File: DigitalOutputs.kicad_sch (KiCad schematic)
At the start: 2 parts, among them J12 DIGITAL_OUTPUTS

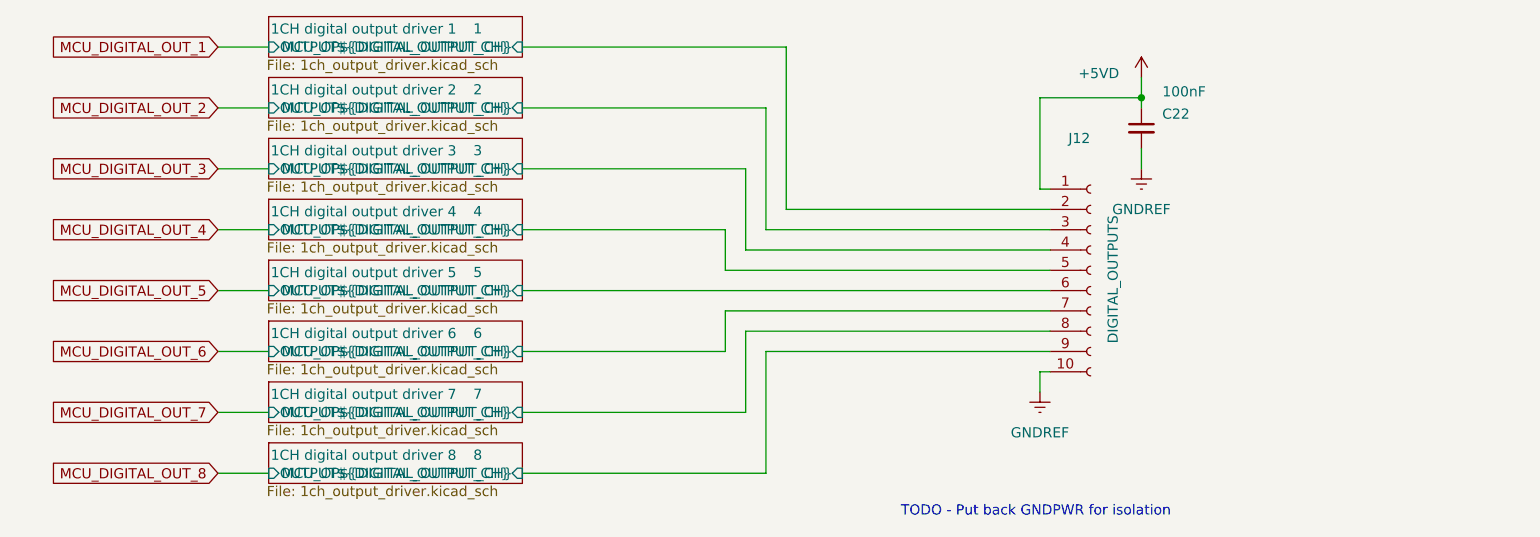
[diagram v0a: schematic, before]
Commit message: New optocoupler part choice, removed digikey BOM as have started inputting them into symbol fields. Re-enabled all disabled parts for now and will re-design power supplies soon.
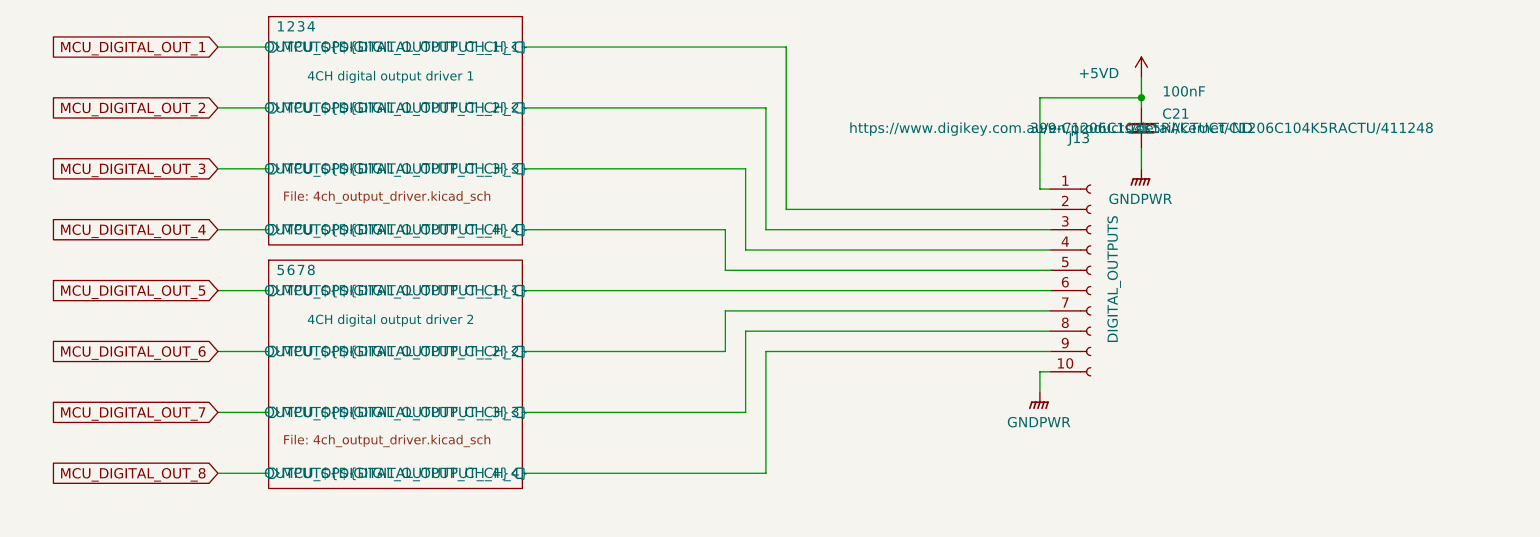
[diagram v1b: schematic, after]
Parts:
- C21: renamed from C22; Digikey Part Number (none) -> 399-C1206C104K5RACTUCT-ND; Digikey URL (none) -> https://www.digikey.com.au/en/products/detail/kemet/C1206C1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
- renumbered J12 to J13
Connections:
- net 4CH digital output driver 1/OUTPUT${DIGITAL_OUTPUT_CH} renamed 4CH digital output driver 1/OUTPUT${DIGITAL_OUTPUT_CH_1}
- net 1CH digital output driver 2/OUTPUT${DIGITAL_OUTPUT_CH} renamed 4CH digital output driver 1/OUTPUT${DIGITAL_OUTPUT_CH_2}
- net 1CH digital output driver 3/OUTPUT${DIGITAL_OUTPUT_CH} renamed 4CH digital output driver 1/OUTPUT${DIGITAL_OUTPUT_CH_3}
- net 1CH digital output driver 4/OUTPUT${DIGITAL_OUTPUT_CH} renamed 4CH digital output driver 1/OUTPUT${DIGITAL_OUTPUT_CH_4}
- net 1CH digital output driver 5/OUTPUT${DIGITAL_OUTPUT_CH} renamed 4CH digital output driver 2/OUTPUT${DIGITAL_OUTPUT_CH_1}
- net 1CH digital output driver 6/OUTPUT${DIGITAL_OUTPUT_CH} renamed 4CH digital output driver 2/OUTPUT${DIGITAL_OUTPUT_CH_2}
- net 1CH digital output driver 7/OUTPUT${DIGITAL_OUTPUT_CH} renamed 4CH digital output driver 2/OUTPUT${DIGITAL_OUTPUT_CH_3}
- net 1CH digital output driver 8/OUTPUT${DIGITAL_OUTPUT_CH} renamed 4CH digital output driver 2/OUTPUT${DIGITAL_OUTPUT_CH_4}
- net GNDREF renamed GNDPWR
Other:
- sheet 1CH digital output driver 1 renamed 4CH digital output driver 1
- removed sheet 1CH digital output driver 2
- removed sheet 1CH digital output driver 3
- removed sheet 1CH digital output driver 4
- removed sheet 1CH digital output driver 5
- removed sheet 1CH digital output driver 6
- removed sheet 1CH digital output driver 7
- removed sheet 1CH digital output driver 8
- added sheet 4CH digital output driver 2 (4ch_output_driver.kicad_sch)
- sheet 4CH digital output driver 1: file 1ch_output_driver.kicad_sch -> 4ch_output_driver.kicad_sch
- sheet 4CH digital output driver 1 ports: added MCU_OP${DIGITAL_OUTPUT_CH_1}, MCU_OP${DIGITAL_OUTPUT_CH_2}, MCU_OP${DIGITAL_OUTPUT_CH_3}, MCU_OP${DIGITAL_OUTPUT_CH_4}, OUTPUT${DIGITAL_OUTPUT_CH_1}, OUTPUT${DIGITAL_OUTPUT_CH_2}, OUTPUT${DIGITAL_OUTPUT_CH_3}, OUTPUT${DIGITAL_OUTPUT_CH_4}; removed MCU_OP${DIGITAL_OUTPUT_CH}, OUTPUT${DIGITAL_OUTPUT_CH}
- note removed: "TODO - Put back GNDPWR for isolation"

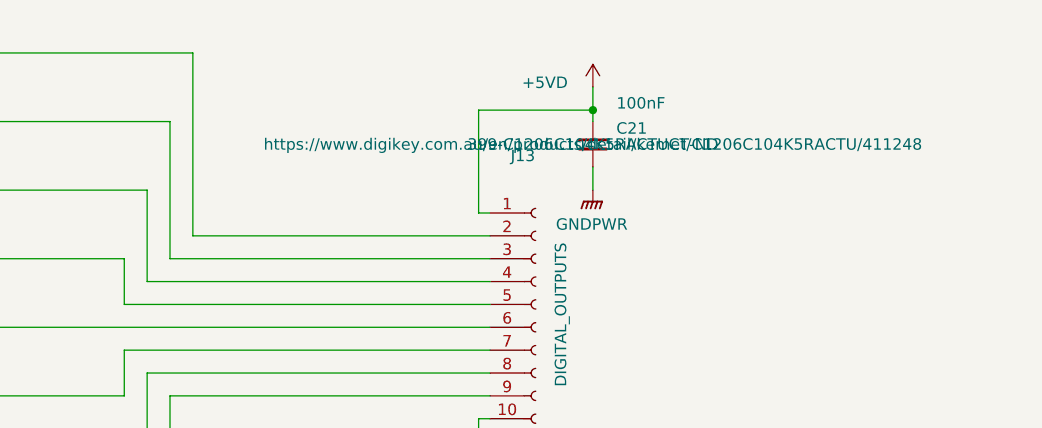
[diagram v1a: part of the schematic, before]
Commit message: fix to annoying additional symbol fields displaying when we didn't want them to.
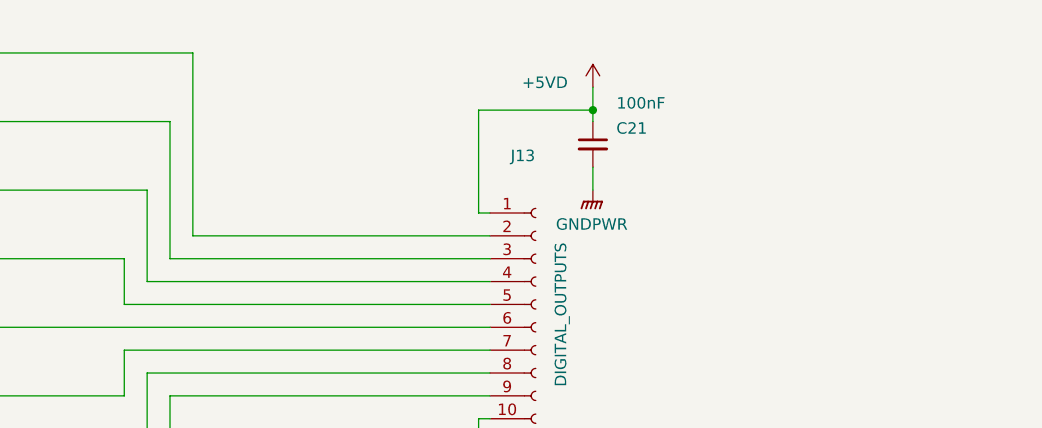
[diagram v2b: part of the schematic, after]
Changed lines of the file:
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@@
 					(size 1.27 1.27)
 				)
+				(hide yes)
 			)
 		)
@@
 					(size 1.27 1.27)
 				)
+				(hide yes)
 			)
 		)
@@
 					(size 1.27 1.27)
 				)
+				(hide yes)
 			)
 		)
@@
 					(size 1.27 1.27)
 				)
-			)
-		)
+				(hide yes)
+			)
+		)

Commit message: BOM consolidation for various resistors. Moved BOM into symbol libraries and updated supplimentary BOM. Switched IO optical isolation circuitry to a more cost effective part.
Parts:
- J13: Digikey Part Number (none) -> See Manual BOM; Digikey URL (none) -> See Manual BOM
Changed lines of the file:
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@@
 			)
 		)
-		(property "Digikey Part Number" ""
+		(property "Digikey Part Number" "See Manual BOM"
 			(at 205.74 93.98 0)
 			(effects
@@
 			)
 		)
-		(property "Digikey URL" ""
+		(property "Digikey URL" "See Manual BOM"
 			(at 205.74 93.98 0)
 			(effects

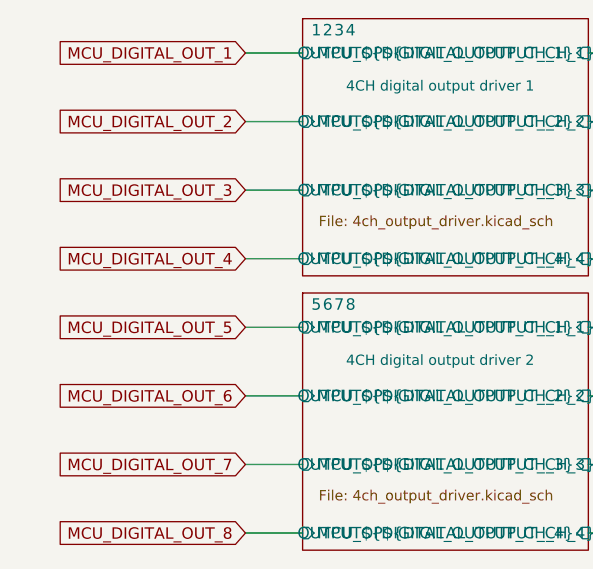
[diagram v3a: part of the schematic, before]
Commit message: Renumbered IO to start at 0 to match firmware
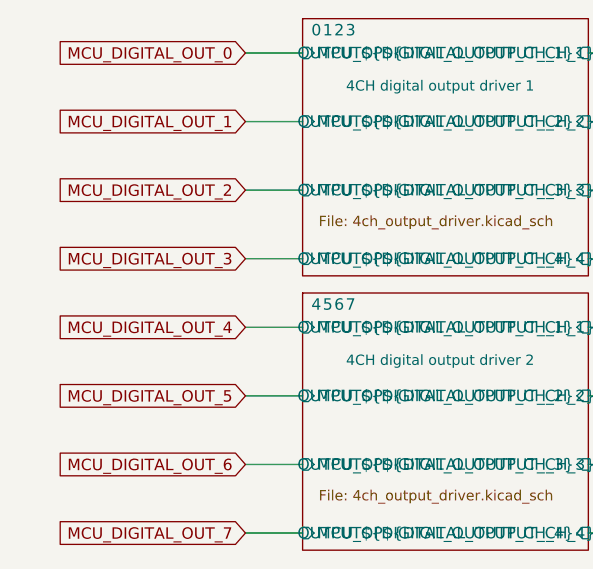
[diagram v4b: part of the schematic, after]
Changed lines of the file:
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@@
 	(global_label "MCU_DIGITAL_OUT_2"
 		(shape input)
-		(at 96.52 73.66 180)
+		(at 96.52 81.28 180)
 		(fields_autoplaced yes)
 		(effects
@@
 		)
 		(property "Intersheetrefs" "${INTERSHEET_REFS}"
-			(at 75.5623 73.66 0)
+			(at 75.5623 81.28 0)
 			(effects
 				(font
@@
 	(global_label "MCU_DIGITAL_OUT_3"
 		(shape input)
-		(at 96.52 81.28 180)
+		(at 96.52 88.9 180)
 		(fields_autoplaced yes)
 		(effects
@@
 		)
 		(property "Intersheetrefs" "${INTERSHEET_REFS}"
-			(at 75.5623 81.28 0)
+			(at 75.5623 88.9 0)
 			(effects
 				(font
@@
 	(global_label "MCU_DIGITAL_OUT_7"
 		(shape input)
-		(at 96.52 111.76 180)
+		(at 96.52 119.38 180)
 		(fields_autoplaced yes)
 		(effects
@@
 		)
 		(property "Intersheetrefs" "${INTERSHEET_REFS}"
-			(at 75.5623 111.76 0)
+			(at 75.5623 119.38 0)
 			(effects
 				(font
@@
 	(global_label "MCU_DIGITAL_OUT_1"
 		(shape input)
-		(at 96.52 66.04 180)
+		(at 96.52 73.66 180)
 		(fields_autoplaced yes)
 		(effects
@@
 		)
 		(property "Intersheetrefs" "${INTERSHEET_REFS}"
-			(at 75.5623 66.04 0)
+			(at 75.5623 73.66 0)
 			(effects
 				(font
@@
 	(global_label "MCU_DIGITAL_OUT_5"
 		(shape input)
-		(at 96.52 96.52 180)
+		(at 96.52 104.14 180)
 		(fields_autoplaced yes)
 		(effects
@@
 		)
 		(property "Intersheetrefs" "${INTERSHEET_REFS}"
-			(at 75.5623 96.52 0)
+			(at 75.5623 104.14 0)
 			(effects
 				(font
@@
 	(global_label "MCU_DIGITAL_OUT_4"
 		(shape input)
-		(at 96.52 88.9 180)
+		(at 96.52 96.52 180)
 		(fields_autoplaced yes)
 		(effects
@@
 		)
 		(property "Intersheetrefs" "${INTERSHEET_REFS}"
-			(at 75.5623 88.9 0)
-			(effects
-				(font
-					(size 1.27 1.27)
-				)
-				(justify right)
-				(hide yes)
-			)
-		)
-	)
-	(global_label "MCU_DIGITAL_OUT_8"
+			(at 75.5623 96.52 0)
+			(effects
+				(font
+					(size 1.27 1.27)
+				)
+				(justify right)
+				(hide yes)
+			)
+		)
+	)
+	(global_label "MCU_DIGITAL_OUT_6"
 		(shape input)
-		(at 96.52 119.38 180)
+		(at 96.52 111.76 180)
 		(fields_autoplaced yes)
 		(effects
@@
 		)
 		(property "Intersheetrefs" "${INTERSHEET_REFS}"
-			(at 75.5623 119.38 0)
-			(effects
-				(font
-					(size 1.27 1.27)
-				)
-				(justify right)
-				(hide yes)
-			)
-		)
-	)
-	(global_label "MCU_DIGITAL_OUT_6"
+			(at 75.5623 111.76 0)
+			(effects
+				(font
+					(size 1.27 1.27)
+				)
+				(justify right)
+				(hide yes)
+			)
+		)
+	)
+	(global_label "MCU_DIGITAL_OUT_0"
 		(shape input)
-		(at 96.52 104.14 180)
+		(at 96.52 66.04 180)
 		(fields_autoplaced yes)
 		(effects
@@
 		)
 		(property "Intersheetrefs" "${INTERSHEET_REFS}"
-			(at 75.5623 104.14 0)
+			(at 75.5623 66.04 0)
 			(effects
 				(font
@@
 			)
 		)
-		(property "DIGITAL_OUTPUT_CH_1" "5"
+		(property "DIGITAL_OUTPUT_CH_1" "4"
 			(at 104.394 93.98 0)
 			(effects
@@
 			)
 		)
-		(property "DIGITAL_OUTPUT_CH_2" "6"
+		(property "DIGITAL_OUTPUT_CH_2" "5"
 			(at 105.664 93.98 0)
 			(effects
@@
 			)
 		)
-		(property "DIGITAL_OUTPUT_CH_3" "7"
+		(property "DIGITAL_OUTPUT_CH_3" "6"
 			(at 106.934 93.98 0)
 			(effects
@@
 			)
 		)
-		(property "DIGITAL_OUTPUT_CH_4" "8"
+		(property "DIGITAL_OUTPUT_CH_4" "7"
 			(at 108.204 93.98 0)
 			(effects
@@
 			)
 		)
-		(property "DIGITAL_OUTPUT_CH_1" "1"
+		(property "DIGITAL_OUTPUT_CH_1" "0"
 			(at 104.394 63.5 0)
 			(effects
@@
 			)
 		)
-		(property "DIGITAL_OUTPUT_CH_2" "2"
+		(property "DIGITAL_OUTPUT_CH_2" "1"
 			(at 105.664 63.5 0)
 			(effects
@@
 			)
 		)
-		(property "DIGITAL_OUTPUT_CH_3" "3"
+		(property "DIGITAL_OUTPUT_CH_3" "2"
 			(at 106.934 63.5 0)
 			(effects
@@
 			)
 		)
-		(property "DIGITAL_OUTPUT_CH_4" "4"
+		(property "DIGITAL_OUTPUT_CH_4" "3"
 			(at 108.204 63.5 0)
 			(effects
